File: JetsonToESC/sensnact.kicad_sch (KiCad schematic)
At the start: 9 parts, among them U2 DS18B20, U5 ACS759ECB-200B-PFF-T

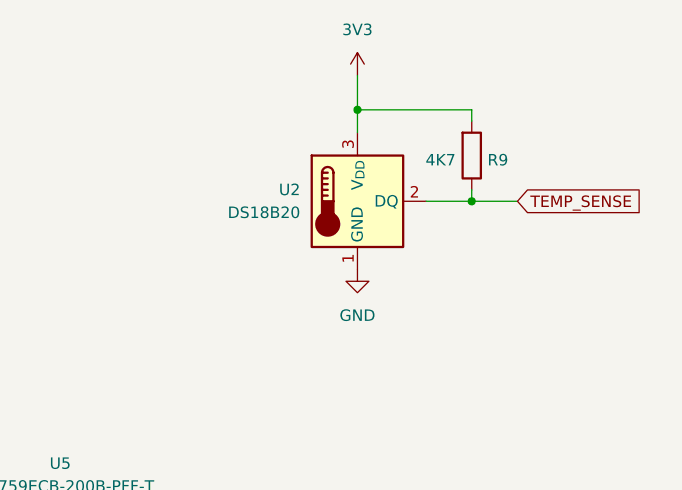
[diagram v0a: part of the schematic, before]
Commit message: Updated connector and temp sensor into IDC and NTC
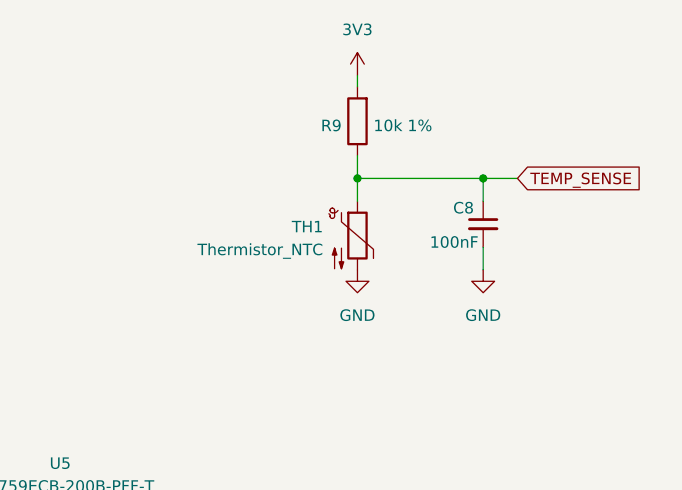
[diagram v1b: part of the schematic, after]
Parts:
- removed U2: DS18B20, Package_TO_SOT_THT:TO-92_Inline, symbol Sensor_Temperature:DS18B20
- added C8: 100nF, Capacitor_SMD:C_0603_1608Metric, symbol Device:C_Small
- added TH1: Thermistor_NTC, Resistor_SMD:R_0805_2012Metric, symbol Device:Thermistor_NTC
- R9: value 4K7 -> 10k 1%
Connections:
- net GND: now also C8.2, TH1.2
- net TEMP_SENSE: now also C8.1, TH1.1
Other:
- moved on the sheet: R9
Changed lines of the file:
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@@
+	)
+	(junction
+		(at 148.59 44.45)
+		(diameter 0)
+		(color 0 0 0 0)
 	)
 	(junction
@@
 	)
 	(junction
-		(at 161.29 46.99)
+		(at 162.56 44.45)
 		(diameter 0)
 		(color 0 0 0 0)
@@
 		(color 0 0 0 0)
 	)
-	(junction
-		(at 148.59 36.83)
-		(diameter 0)
-		(color 0 0 0 0)
-	)
 	(wire
 		(pts
@@
 	(wire
 		(pts
-			(xy 148.59 33.02) (xy 148.59 36.83)
+			(xy 148.59 33.02) (xy 148.59 34.29)
 		)
 		(stroke
@@
 	(wire
 		(pts
+			(xy 162.56 44.45) (xy 148.59 44.45)
+		)
+		(stroke
+			(width 0)
+			(type default)
+		)
+	)
+	(wire
+		(pts
 			(xy 54.61 43.18) (xy 54.61 45.72)
 		)
@@
 	(wire
 		(pts
+			(xy 162.56 44.45) (xy 162.56 46.99)
+		)
+		(stroke
+			(width 0)
+			(type default)
+		)
+	)
+	(wire
+		(pts
 			(xy 120.65 90.17) (xy 120.65 92.71)
 		)
@@
 	(wire
 		(pts
-			(xy 161.29 45.72) (xy 161.29 46.99)
+			(xy 148.59 41.91) (xy 148.59 44.45)
 		)
 		(stroke
@@
 	(wire
 		(pts
-			(xy 161.29 38.1) (xy 161.29 36.83)
-		)
-		(stroke
-			(width 0)
-			(type default)
-		)
-	)
-	(wire
-		(pts
-			(xy 161.29 36.83) (xy 148.59 36.83)
-		)
-		(stroke
-			(width 0)
-			(type default)
-		)
-	)
-	(wire
-		(pts
 			(xy 95.25 72.39) (xy 95.25 74.93)
 		)
@@
 	(wire
 		(pts
-			(xy 148.59 36.83) (xy 148.59 39.37)
+			(xy 148.59 44.45) (xy 148.59 46.99)
 		)
 		(stroke
@@
 	(wire
 		(pts
-			(xy 161.29 46.99) (xy 156.21 46.99)
-		)
-		(stroke
-			(width 0)
-			(type default)
-		)
-	)
-	(wire
-		(pts
 			(xy 81.28 80.01) (xy 85.09 80.01)
 		)
@@
 	(wire
 		(pts
-			(xy 166.37 46.99) (xy 161.29 46.99)
+			(xy 162.56 52.07) (xy 162.56 54.61)
+		)
+		(stroke
+			(width 0)
+			(type default)
+		)
+	)
+	(wire
+		(pts
+			(xy 166.37 44.45) (xy 162.56 44.45)
 		)
 		(stroke
@@
 	(global_label "TEMP_SENSE"
 		(shape input)
-		(at 166.37 46.99 0)
+		(at 166.37 44.45 0)
 		(fields_autoplaced yes)
 		(effects
@@
 		)
 		(property "Intersheetrefs" "${INTERSHEET_REFS}"
-			(at 181.2083 46.99 0)
+			(at 181.2083 44.45 0)
 			(effects
 				(font
@@
 	)
 	(symbol
-		(lib_id "Sensor_Temperature:DS18B20")
-		(at 148.59 46.99 0)
-		(unit 1)
-		(exclude_from_sim no)
-		(in_bom yes)
-		(on_board yes)
-		(dnp no)
-		(property "Reference" "U2"
-			(at 142.24 45.7199 0)
-			(effects
-				(font
-					(size 1.27 1.27)
-				)
-				(justify right)
-			)
-		)
-		(property "Value" "DS18B20"
-			(at 142.24 48.2599 0)
-			(effects
-				(font
-					(size 1.27 1.27)
-				)
-				(justify right)
-			)
-		)
-		(property "Footprint" "Package_TO_SOT_THT:TO-92_Inline"
-			(at 123.19 53.34 0)
-			(effects
-				(font
-					(size 1.27 1.27)
-				)
-				(hide yes)
-			)
-		)
-		(property "Datasheet" "http://datasheets.maximintegrated.com/en/ds/DS18B20.pdf"
-			(at 144.78 40.64 0)
-			(effects
-				(font
-					(size 1.27 1.27)
-				)
-				(hide yes)
-			)
-		)
-		(property "Description" "Programmable Resolution 1-Wire Digital Thermometer TO-92"
-			(at 148.59 46.99 0)
-			(effects
-				(font
-					(size 1.27 1.27)
-				)
-				(hide yes)
-			)
-		)
-		(pin "1"
-		)
-		(pin "2"
-		)
-		(pin "3"
-		)
-		(instances
-			(project "JetsonToESC"
-				(path "/47af999a-55f7-4333-ac4c-b272b7fb2895/0909a279-36d6-41ad-844b-878e1aabe858"
-					(reference "U2")
-					(unit 1)
-				)
-			)
-		)
-	)
-	(symbol
 		(lib_id "Device:C_Small")
 		(at 100.33 72.39 270)
@@
 	(symbol
 		(lib_id "Device:R")
-		(at 161.29 41.91 0)
-		(mirror x)
+		(at 148.59 38.1 180)
 		(unit 1)
 		(exclude_from_sim no)
@@
 		(dnp no)
 		(property "Reference" "R9"
-			(at 165.354 42.418 0)
+			(at 144.526 38.608 0)
 			(effects
 				(font
@@
 			)
 		)
-		(property "Value" "4K7"
-			(at 159.512 42.418 0)
+		(property "Value" "10k 1%"
+			(at 150.368 38.608 0)
 			(effects
 				(font
@@
 		)
 		(property "Footprint" "Resistor_SMD:R_0603_1608Metric"
-			(at 159.512 41.91 90)
+			(at 150.368 38.1 90)
 			(effects
 				(font
@@
 		)
 		(property "Datasheet" "~"
-			(at 161.29 41.91 0)
+			(at 148.59 38.1 0)
 			(effects
 				(font
@@
 		)
 		(property "Description" "Resistor"
-			(at 161.29 41.91 0)
+			(at 148.59 38.1 0)
 			(effects
 				(font
@@
 	)
 	(symbol
+		(lib_id "power:GND")
+		(at 162.56 54.61 0)
+		(mirror y)
+		(unit 1)
+		(exclude_from_sim no)
+		(in_bom yes)
+		(on_board yes)
+		(dnp no)
+		(fields_autoplaced yes)
+		(property "Reference" "#PWR010"
+			(at 162.56 60.96 0)
+			(effects
+				(font
+					(size 1.27 1.27)
+				)
+				(hide yes)
+			)
+		)
+		(property "Value" "GND"
+			(at 162.56 59.69 0)
+			(effects
+				(font
+					(size 1.27 1.27)
+				)
+			)
+		)
+		(property "Footprint" ""
+			(at 162.56 54.61 0)
+			(effects
+				(font
+					(size 1.27 1.27)
+				)
+				(hide yes)
+			)
+		)
+		(property "Datasheet" ""
+			(at 162.56 54.61 0)
+			(effects
+				(font
+					(size 1.27 1.27)
+				)
+				(hide yes)
+			)
+		)
+		(property "Description" "Power symbol creates a global label with name \"GND\" , ground"
+			(at 162.56 54.61 0)
+			(effects
+				(font
+					(size 1.27 1.27)
+				)
+				(hide yes)
+			)
+		)
+		(pin "1"
+		)
+		(instances
+			(project "JetsonToESC"
+				(path "/47af999a-55f7-4333-ac4c-b272b7fb2895/0909a279-36d6-41ad-844b-878e1aabe858"
+					(reference "#PWR010")
+					(unit 1)
+				)
+			)
+		)
+	)
+	(symbol
 		(lib_id "power:VCC")
 		(at 148.59 33.02 0)
@@
 	)
 	(symbol
+		(lib_id "Device:C_Small")
+		(at 162.56 49.53 0)
+		(mirror y)
+		(unit 1)
+		(exclude_from_sim no)
+		(in_bom yes)
+		(on_board yes)
+		(dnp no)
+		(property "Reference" "C8"
+			(at 161.544 47.752 0)
+			(effects
+				(font
+					(size 1.27 1.27)
+				)
+				(justify left)
+			)
+		)
+		(property "Value" "100nF"
+			(at 162.052 51.562 0)
+			(effects
+				(font
+					(size 1.27 1.27)
+				)
+				(justify left)
+			)
+		)
+		(property "Footprint" "Capacitor_SMD:C_0603_1608Metric"
+			(at 162.56 49.53 0)
+			(effects
+				(font
+					(size 1.27 1.27)
+				)
+				(hide yes)
+			)
+		)
+		(property "Datasheet" "~"
+			(at 162.56 49.53 0)
+			(effects
+				(font
+					(size 1.27 1.27)
+				)
+				(hide yes)
+			)
+		)
+		(property "Description" ""
+			(at 162.56 49.53 0)
+			(effects
+				(font
+					(size 1.27 1.27)
+				)
+			)
+		)
+		(pin "1"
+		)
+		(pin "2"
+		)
+		(instances
+			(project "JetsonToESC"
+				(path "/47af999a-55f7-4333-ac4c-b272b7fb2895/0909a279-36d6-41ad-844b-878e1aabe858"
+					(reference "C8")
+					(unit 1)
+				)
+			)
+		)
+	)
+	(symbol
 		(lib_id "power:GND")
 		(at 102.87 72.39 90)
@@
 					(unit 1)
 				)
+			)
+		)
+	)
+	(symbol
+		(lib_id "Device:Thermistor_NTC")
+		(at 148.59 50.8 0)
+		(unit 1)
+		(exclude_from_sim no)
+		(in_bom yes)
+		(on_board yes)
+		(dnp no)
+		(property "Reference" "TH1"
+			(at 144.78 49.8474 0)
+			(effects
+				(font
+					(size 1.27 1.27)
+				)
+				(justify right)
+			)
+		)
+		(property "Value" "Thermistor_NTC"
+			(at 144.78 52.3874 0)
+			(effects
+				(font
+					(size 1.27 1.27)
+				)
+				(justify right)
+			)
+		)
+		(property "Footprint" "Resistor_SMD:R_0805_2012Metric"
+			(at 148.59 49.53 0)
+			(effects
+				(font
+					(size 1.27 1.27)
+				)
+				(hide yes)
+			)
+		)
+		(property "Datasheet" "~"
+			(at 148.59 49.53 0)
+			(effects
+				(font
+					(size 1.27 1.27)
+				)
+				(hide yes)
+			)
+		)
+		(property "Description" "Temperature dependent resistor, negative temperature coefficient"
+			(at 148.59 50.8 0)
+			(effects
+				(font
+					(size 1.27 1.27)
+				)
+				(hide yes)
+			)
+		)
+		(pin "2"
+		)
+		(pin "1"
+		)
+		(instances
+			(project "JetsonToESC"
+				(path "/47af999a-55f7-4333-ac4c-b272b7fb2895/0909a279-36d6-41ad-844b-878e1aabe858"
+					(reference "TH1")
+					(unit 1)
+				)
